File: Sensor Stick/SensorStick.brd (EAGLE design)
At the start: 100 x 80 mm, 15 parts, among them U2 BME280, U3 MLX90614_

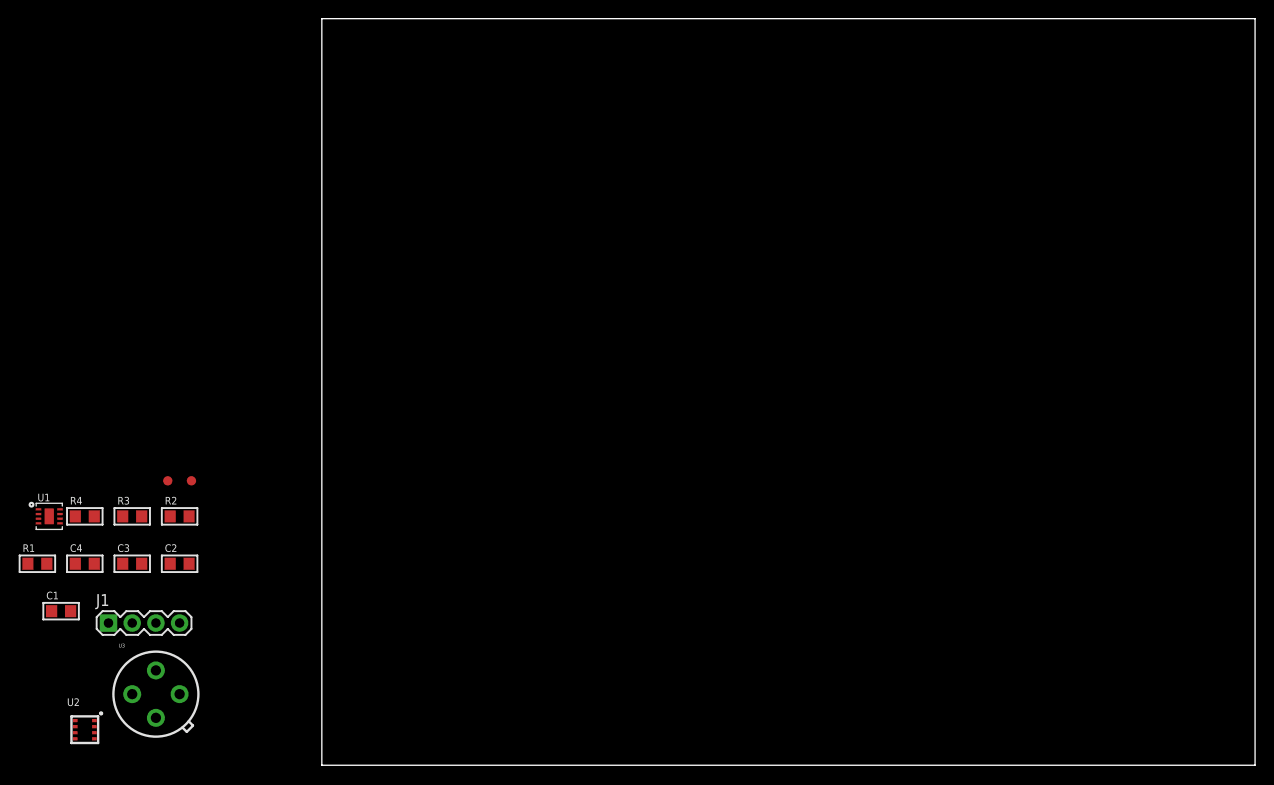
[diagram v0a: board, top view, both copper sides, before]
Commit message: Finished routing sensor stick
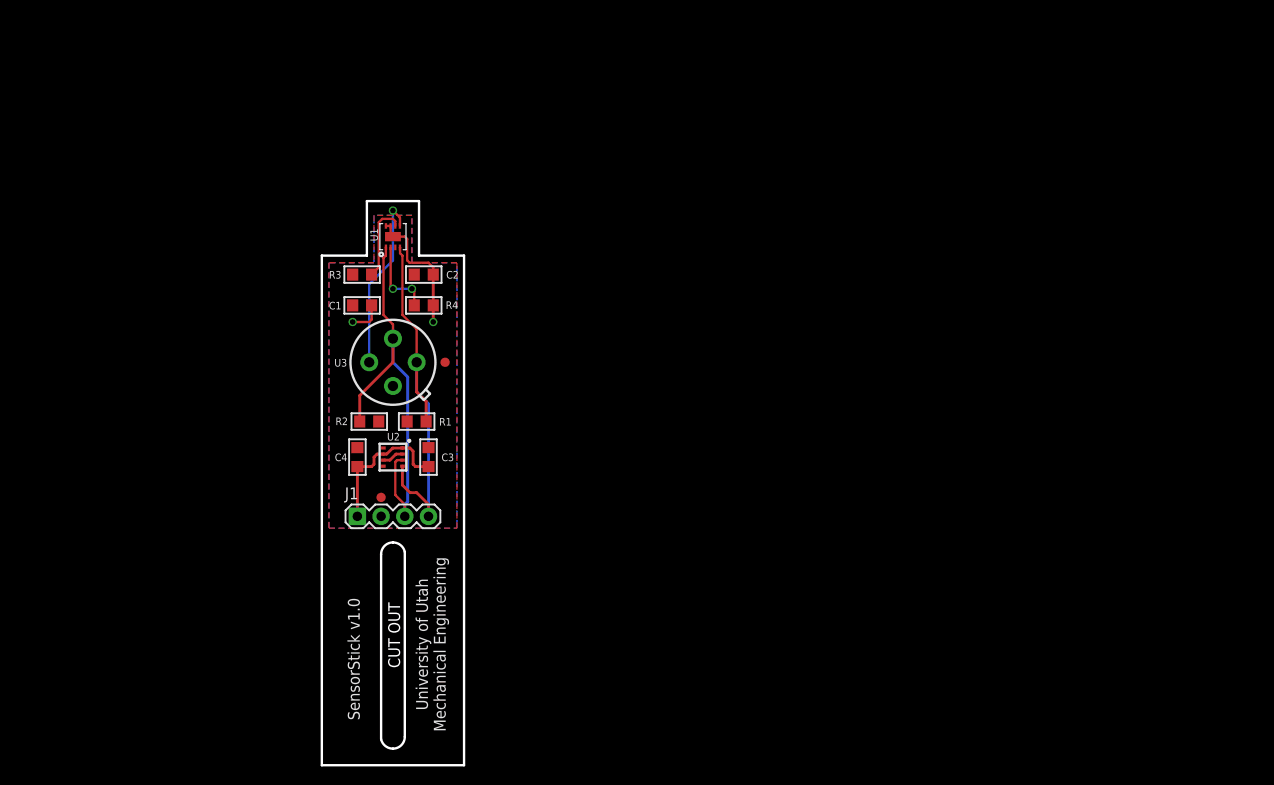
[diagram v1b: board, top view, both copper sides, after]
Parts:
- moved U1 47.5 mm to (7.62, 56.6), turned to 90 degrees
- moved C1 46.0 mm to (4.32, 49.3), turned to 180 degrees
- moved U2 44.1 mm to (7.62, 33.0)
- moved U3 43.7 mm to (7.62, 43.2)
- moved R1 43.4 mm to (10.2, 36.8), turned to 180 degrees
- moved R4 42.8 mm to (10.9, 49.3)
- moved C2 40.6 mm to (10.9, 52.6), turned to 180 degrees
- moved FRAME1 35.9 mm to (0.00, 0.00)
- moved R3 35.8 mm to (4.32, 52.6), turned to 180 degrees
- moved C3 33.7 mm to (11.4, 33.0), turned to 90 degrees
- moved FID2 32.3 mm to (13.2, 43.2)
- moved C4 31.4 mm to (3.81, 33.0), turned to 90 degrees
- moved J1 29.0 mm to (3.81, 26.7)
- moved R2 22.7 mm to (5.08, 36.8)
- moved FID1 20.4 mm to (6.35, 28.7)
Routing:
- net SDA: track 0.00 -> 47.6 mm
- net SCL: track 0.00 -> 43.8 mm
- net GND: track 0.00 -> 34.1 mm, vias 0 -> 2
- net 3.3V: track 0.00 -> 21.6 mm, vias 0 -> 1
- net ADDR: track 0.00 -> 8.46 mm, vias 0 -> 2
- net RST: track 0.00 -> 8.44 mm
- added copper zone on layer 1, net 3.3V
- added copper zone on layer 16, net GND
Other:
- board size 100 x 80 mm -> 15.2 x 60.5 mm
- board text added: "CUT OUT"
- board text added: "SensorStick v1.0"
- board text added: "University of Utah Mechanical Engineering"
